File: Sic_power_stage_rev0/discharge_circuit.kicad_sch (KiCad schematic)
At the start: 25 parts, among them Q19 IPN70R1K5CEATMA1

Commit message: Add changes in power stage
 - Redefine DC-link capacitor size per leg.
 - Change footprint SiC MOSFET.
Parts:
- removed C28: C-0603, IPC7351-Nominal:CAPC1608X55, symbol pasv-cap:C-0603
- removed DS1: LED, symbol _semi:LED
- removed Q19: IPN70R1K5CEATMA1, smd-semi:SOT-223-3, symbol semi-trans-Infineon:IPN70R1K5CEATMA1
- removed R46, R47, R48, R52, R53, R54, R55, R56, R57, R58, R59, R60, R61, R62, R63, R64, R65, R66, R67, R68, R69: R-1206, IPC7351-Nominal:RESC3216X60, symbol pasv-res:R-1206
- removed R70: R-0603, IPC7351-Nominal:RESC1608X50, symbol pasv-res:R-0603

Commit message: Add changes
 - Add DC-LINK capacitor discharge circuit.
 - VBUS resistive divider.
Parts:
- added C40: 100nF, IPC7351-Nominal:CAPC1608X55, symbol pasv-cap:C-0603
- added C41: C-0603, IPC7351-Nominal:CAPC1608X55, symbol pasv-cap:C-0603
- added D13: SMAJ5.0A, Diode_SMD:D_SMA, symbol Diode:SMAJ5.0A
- added DS1: LED-0603, smd-semi:LED-0603, symbol semi-opto-generic:LED-0603
- added Q13: IPN70R1K5CEATMA1, smd-semi:SOT-223-3, symbol semi-trans-Infineon:IPN70R1K5CEATMA1
- added R1, R2, R3, R34, R35, R36, R37, R38, R39, R40, R41, R42, R43, R44, R45, R46, R47, R48: R-1206, IPC7351-Nominal:RESC3216X60, symbol pasv-res:R-1206
- added U1: TLP785, Package_DIP:DIP-4_W7.62mm, symbol Isolator:TLP785
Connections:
- new net: R48.1, U1.1
- new net: D13.1 (A1), R46.1, R47.1, U1.4
- new net: C41.1, Q13.1 (G), R47.2
- new net: R2.1, R3.1, R37.1, R38.2, R39.2, R40.2
- new net: R38.1, R39.1, R40.1, R41.2, R42.2, R43.2
- new net: R45.1, R46.2
- new net: R44.2, R45.2
- new net: DS1.2 (A), R41.1, R42.1, R43.1, R44.1
- new net: DS1.1 (K), Q13.2 (S)
- new net: R34.1, R35.2
- new net: R34.2, R36.1
- new net 3.3V+: R48.2
- new net GND: U1.2
- new net PWRGND: C40.2, C41.2, D13.2 (A2), Q13.3 (D), R1.1, U1.3
- new net VBUS: R2.2, R3.2, R36.2, R37.2
- new net VBUS_LOW: C40.1, R1.2, R35.1
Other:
- note added: "120K resistor ensure a dischrge voltage less than 60V in 2.4 seg"
- note added: "Resistor par number CRMA1206AF120KFKEF"
- note added: "TDB"
- note added: "chose a ratio resistor to reduce the 400V to less than 60V. To be matched with the Amphenol crearance connector."
- note added: "signals comming from the controller"

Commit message: SiC: routing phase A and B - place components
Signed-off-by: Ayarde Christian <cayarde@paltatech.com>
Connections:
- net VBUS_LOW: now also R34.1; no longer R35.1
- net at R35.2: now also R36.1; no longer R34.1
- net at R34.2: now also R35.1; no longer R36.1
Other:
- moved on the sheet: R34, R35
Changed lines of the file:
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@@
 	(symbol
 		(lib_id "pasv-res:R-1206")
-		(at 115.57 54.61 180)
+		(at 115.57 63.5 180)
 		(unit 1)
 		(exclude_from_sim no)
@@
 		(dnp no)
 		(property "Reference" "R34"
-			(at 112.776 52.832 90)
+			(at 112.776 61.722 90)
 			(effects
 				(font
@@
 		)
 		(property "Value" "R-1206"
-			(at 113.03 53.3084 0)
+			(at 113.03 62.1984 0)
 			(effects
 				(font
@@
 		)
 		(property "Footprint" "IPC7351-Nominal:RESC3216X60"
-			(at 115.57 54.61 0)
-			(effects
-				(font
-					(size 1.27 1.27)
-				)
-				(hide yes)
-			)
-		)
-		(property "Datasheet" ""
-			(at 115.57 55.88 0)
+			(at 115.57 63.5 0)
+			(effects
+				(font
+					(size 1.27 1.27)
+				)
+				(hide yes)
+			)
+		)
+		(property "Datasheet" ""
+			(at 115.57 64.77 0)
 			(effects
 				(font
@@
 		)
 		(property "Description" "Chip resistor, EIA 1206, metric 3216"
-			(at 115.57 54.61 0)
+			(at 115.57 63.5 0)
 			(effects
 				(font
@@
 		)
 		(property "BOM" "RES SMD 1k 5% [1206]"
-			(at 96.52 68.58 0)
+			(at 96.52 77.47 0)
 			(effects
 				(font
@@
 	(symbol
 		(lib_id "pasv-res:R-1206")
-		(at 115.57 63.5 180)
+		(at 115.57 54.61 180)
 		(unit 1)
 		(exclude_from_sim no)
@@
 		(dnp no)
 		(property "Reference" "R35"
-			(at 112.776 61.468 90)
+			(at 112.776 52.578 90)
 			(effects
 				(font
@@
 		)
 		(property "Value" "R-1206"
-			(at 113.03 62.1984 0)
+			(at 113.03 53.3084 0)
 			(effects
 				(font
@@
 		)
 		(property "Footprint" "IPC7351-Nominal:RESC3216X60"
-			(at 115.57 63.5 0)
-			(effects
-				(font
-					(size 1.27 1.27)
-				)
-				(hide yes)
-			)
-		)
-		(property "Datasheet" ""
-			(at 115.57 64.77 0)
+			(at 115.57 54.61 0)
+			(effects
+				(font
+					(size 1.27 1.27)
+				)
+				(hide yes)
+			)
+		)
+		(property "Datasheet" ""
+			(at 115.57 55.88 0)
 			(effects
 				(font
@@
 		)
 		(property "Description" "Chip resistor, EIA 1206, metric 3216"
-			(at 115.57 63.5 0)
+			(at 115.57 54.61 0)
 			(effects
 				(font
@@
 		)
 		(property "BOM" "RES SMD 1k 5% [1206]"
-			(at 96.52 77.47 0)
-			(effects
-				(font
+			(at 96.52 68.58 0)
+			(effects
+				(font

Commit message: Sic: Add vias on leg B
Signed-off-by: Ayarde Christian <cayarde@paltatech.com>
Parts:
- R48: footprint IPC7351-Nominal:RESC3216X60 -> Resistor_SMD:R_0603_1608Metric
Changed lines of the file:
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@@
 			)
 		)
-		(property "Footprint" "IPC7351-Nominal:RESC3216X60"
+		(property "Footprint" "Resistor_SMD:R_0603_1608Metric"
 			(at 101.6 109.22 0)
 			(effects

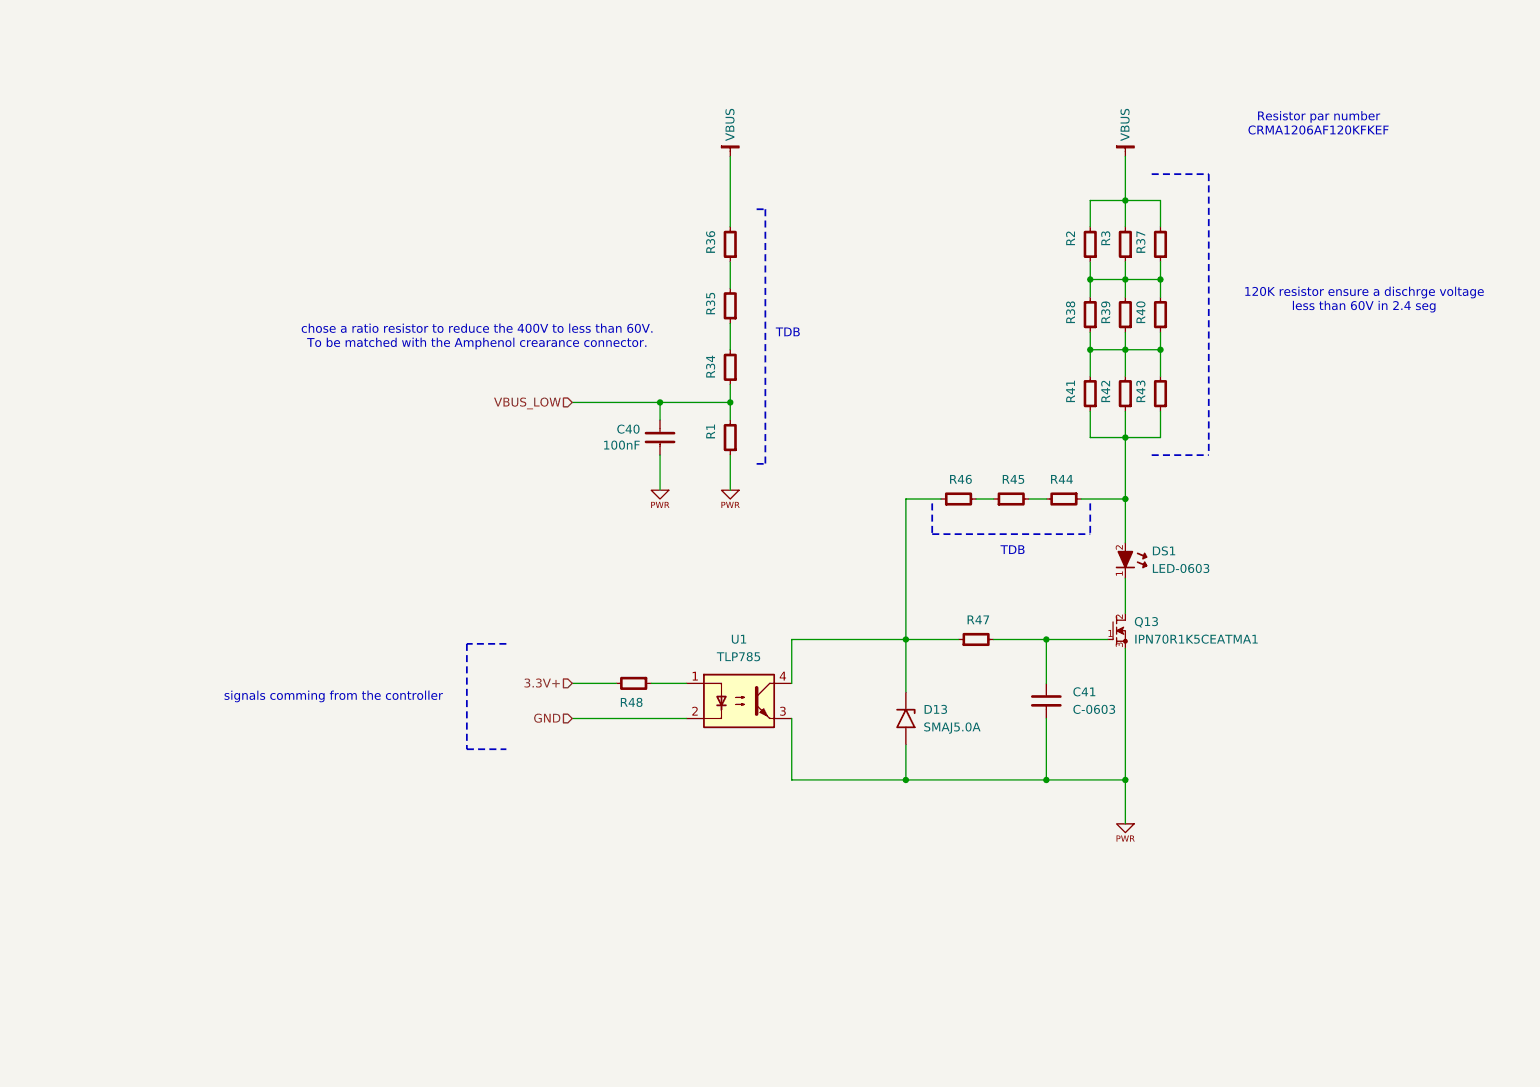
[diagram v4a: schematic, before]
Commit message: Sic: define resistors value for discharge circuit
Signed-off-by: Ayarde Christian <cayarde@paltatech.com>
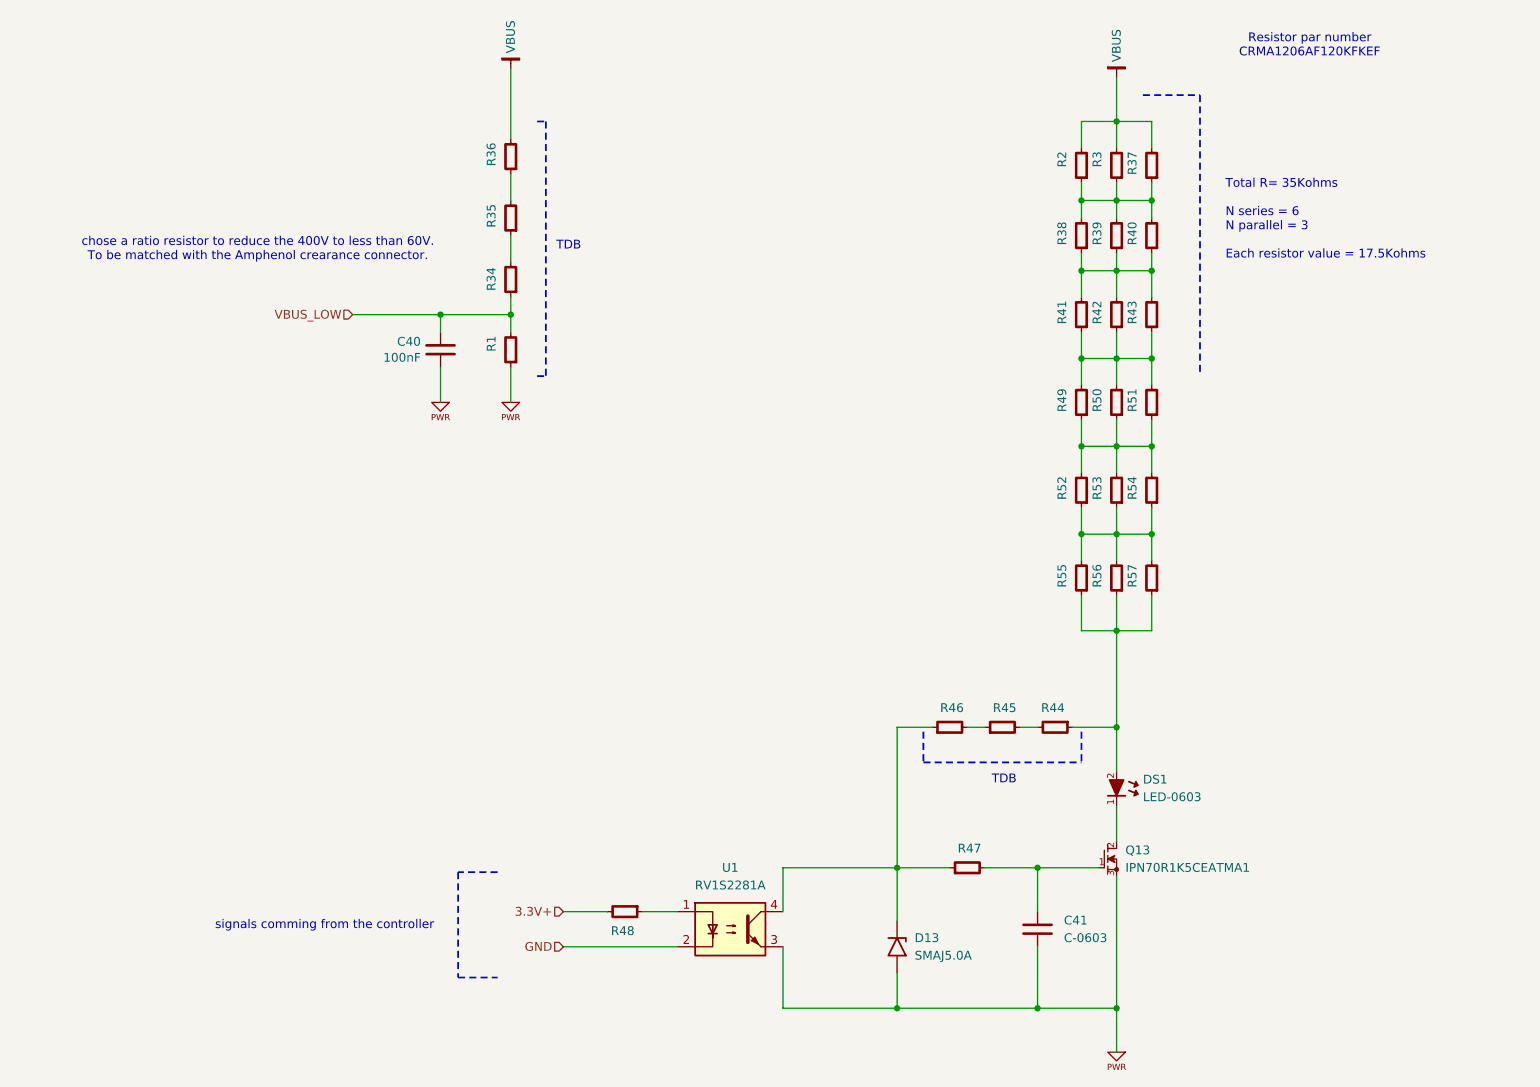
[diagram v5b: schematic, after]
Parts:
- added R49, R50, R51, R52, R53, R54, R55, R56, R57: R-1206, IPC7351-Nominal:RESC3216X60, symbol pasv-res:R-1206
- R2: BOM RES SMD 1k 5% [1206] -> RES SMD 17.6k 5% [1206]; MFR (none) -> Stackpole Electronics Inc; MPN (none) -> RNCF1206BKE17K6
- U1: value TLP785 -> RV1S2281A; footprint Package_DIP:DIP-4_W7.62mm -> Package_SO:SSOP-4_4.4x2.6mm_P1.27mm; BOM (none) -> OPTOISOLTR 5KV 1CH TRANS 4-LSSOP; MFR (none) -> Renesas Electronics Corporation; MPN (none) -> RV1S2281ACCSP-10YC#SC0
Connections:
- net at R41.1, R42.1, R43.1: now also R49.2, R50.2, R51.2; no longer DS1.2 (A), R44.1
- new net: DS1.2 (A), R44.1, R55.1, R56.1, R57.1
- new net: R52.1, R53.1, R54.1, R55.2, R56.2, R57.2
- new net: R49.1, R50.1, R51.1, R52.2, R53.2, R54.2
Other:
- note added: "Total R= 35Kohms N series = 6 N parallel = 3 Each resistor value = 17.5Kohms"
- note removed: "120K resistor ensure a dischrge voltage less than 60V in 2.4 seg"
- moved on the sheet: C40, C41, D13, DS1, Q13, R1, R2, R3, R34, R35, R36, R37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

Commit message: Sic: Define custom rules for Vbus sense
Signed-off-by: Ayarde Christian <cayarde@paltatech.com>
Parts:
- C41: value C-0603 -> 100n
- R1: value R-1206 -> 5K; footprint IPC7351-Nominal:RESC3216X60 -> Resistor_SMD:R_0603_1608Metric
- R2: value R-1206 -> 17.6K
- R3, R37, R38, R39, R40, R41, R42, R43, R49, R50, R51, R52, R53, R54, R55, R56, R57: value R-1206 -> 17.6K; BOM RES SMD 1k 5% [1206] -> RES SMD 17.6k 5% [1206]; MFR (none) -> Stackpole Electronics Inc; MPN (none) -> RNCF1206BKE17K6
- R34, R35, R36: value R-1206 -> 220K
- R44, R45, R46: value R-1206 -> 365K; BOM RES SMD 1k 5% [1206] -> RES SMD 365K OHM 1% 1/4W 1206; MFR (none) -> Vishay Dale; MPN (none) -> CRCW1206365KFKEA
- R47: value R-1206 -> 10R; footprint IPC7351-Nominal:RESC3216X60 -> Resistor_SMD:R_0805_2012Metric; BOM RES SMD 1k 5% [1206] -> RES SMD 10 OHM 1% 1/4W 0805; MFR (none) -> Vishay Dale; MPN (none) -> CRCW080510R0FKEA
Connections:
- net PHASE_HV_A_2: now reaches R34.2, R35.1
- net PHASE_HV_A_1: now reaches R35.2, R36.1
